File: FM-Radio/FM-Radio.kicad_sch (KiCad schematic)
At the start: 60 parts, among them J1 L_OUT, J2 USB_C_Receptacle_USB2.0, J3 R_OUT, J4 VBUS, J5 GND, J6 BWSMA-KE-Z001, SW2 EN, U2 SI4702-C19-GMR, U3 ESP32-S3-MINI-1, U4 PRTR5V0U2X, U5 TPS62160DSG, U6 PAM8406D, Y1 32.768 kHz

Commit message: RAAAA
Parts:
- C1, C3: LCSC C15850 -> C440198
- C15: LCSC Part # C72498 -> C3340
- C23: LCSC Part # C15850 -> C440198
- C25: LCSC Part # C1791 -> C46653
- R10, R3: LCSC Part # C17414 -> C17673
- R2: LCSC Part # C84376 -> C17414
- U6: LCSC Part # (none) -> C86270
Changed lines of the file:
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@@
 			)
 		)
-		(property "LCSC Part #" "C15850"
+		(property "LCSC Part #" "C440198"
 			(at 200.66 130.81 0)
 			(effects
@@
 			)
 		)
-		(property "LCSC Part #" "C17414"
+		(property "LCSC Part #" "C17673"
 			(at 81.28 156.21 0)
 			(effects
@@
 			)
 		)
-		(property "LCSC" "C15850"
+		(property "LCSC" "C440198"
 			(at 143.51 30.48 0)
 			(effects
@@
 			)
 		)
+		(property "LCSC Part #" "C86270"
+			(at 157.48 74.93 0)
+			(effects
+				(font
+					(size 1.27 1.27)
+				)
+				(hide yes)
+			)
+		)
 		(pin "5"
 		)
@@
 			)
 		)
-		(property "LCSC Part #" "C84376"
+		(property "LCSC Part #" "C17414"
 			(at 24.13 52.07 0)
 			(effects
@@
 			)
 		)
-		(property "LCSC Part #" "C72498"
+		(property "LCSC Part #" "C3340"
 			(at 130.81 30.48 0)
 			(effects
@@
 			)
 		)
-		(property "LCSC" "C15850"
+		(property "LCSC" "C440198"
 			(at 215.9 30.48 0)
 			(effects
@@
 			)
 		)
-		(property "LCSC Part #" "C1791"
+		(property "LCSC Part #" "C46653"
 			(at 15.24 33.02 0)
 			(effects
@@
 			)
 		)
-		(property "LCSC Part #" "C17414"
+		(property "LCSC Part #" "C17673"
 			(at 88.9 158.75 0)
 			(effects

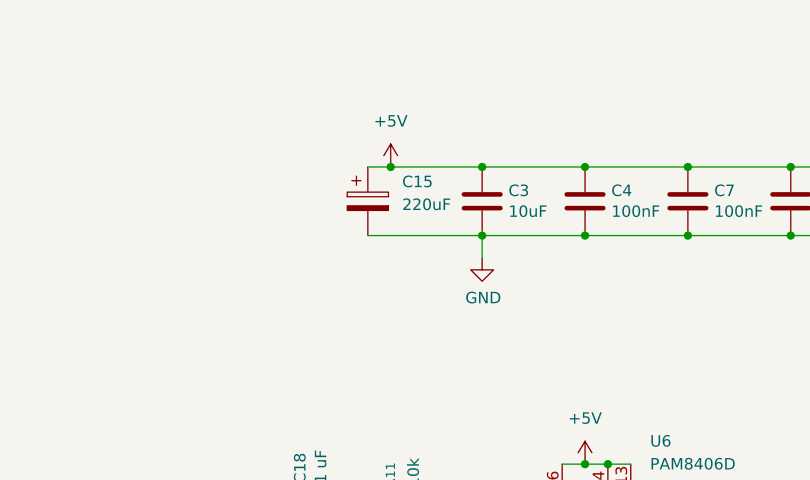
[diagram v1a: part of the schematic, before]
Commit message: FM radio
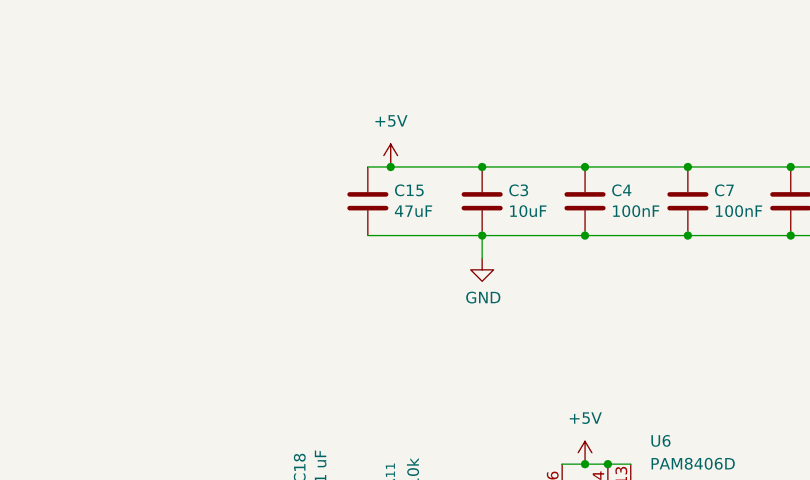
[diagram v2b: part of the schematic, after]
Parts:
- removed C15: 220uF, Capacitor_SMD:C_Elec_8x10.2, symbol Device:C_Polarized
- added C15: 47uF, Capacitor_SMD:C_1206_3216Metric, symbol Device:C
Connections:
- net +5V: now also C15.1
- net GND: now also C15.2
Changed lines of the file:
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@@
+	)
+	(symbol
+		(lib_id "Device:C")
+		(at 130.81 30.48 0)
+		(unit 1)
+		(exclude_from_sim no)
+		(in_bom yes)
+		(on_board yes)
+		(dnp no)
+		(property "Reference" "C15"
+			(at 133.731 29.3116 0)
+			(effects
+				(font
+					(size 1.27 1.27)
+				)
+				(justify left)
+			)
+		)
+		(property "Value" "47uF"
+			(at 133.731 31.623 0)
+			(effects
+				(font
+					(size 1.27 1.27)
+				)
+				(justify left)
+			)
+		)
+		(property "Footprint" "Capacitor_SMD:C_1206_3216Metric"
+			(at 131.7752 34.29 0)
+			(effects
+				(font
+					(size 1.27 1.27)
+				)
+				(hide yes)
+			)
+		)
+		(property "Datasheet" "~"
+			(at 130.81 30.48 0)
+			(effects
+				(font
+					(size 1.27 1.27)
+				)
+				(hide yes)
+			)
+		)
+		(property "Description" ""
+			(at 130.81 30.48 0)
+			(effects
+				(font
+					(size 1.27 1.27)
+				)
+			)
+		)
+		(property "LCSC" "C96123"
+			(at 130.81 30.48 0)
+			(effects
+				(font
+					(size 1.27 1.27)
+				)
+				(hide yes)
+			)
+		)
+		(property "JlcRotOffset" ""
+			(at 130.81 30.48 0)
+			(effects
+				(font
+					(size 1.27 1.27)
+				)
+				(hide yes)
+			)
+		)
+		(pin "1"
+		)
+		(pin "2"
+		)
+		(instances
+			(project "FM-Radio"
+				(path "/8a5dac2c-def6-4068-997d-88e941bc9e21"
+					(reference "C15")
+					(unit 1)
+				)
+			)
+		)
 	)
 	(symbol
@@
 					(unit 1)
 				)
-			)
-		)
-	)
-	(symbol
-		(lib_id "Device:C_Polarized")
-		(at 130.81 30.48 0)
-		(unit 1)
-		(exclude_from_sim no)
-		(in_bom yes)
-		(on_board yes)
-		(dnp no)
-		(fields_autoplaced yes)
-		(property "Reference" "C15"
-			(at 134.62 28.3209 0)
-			(effects
-				(font
-					(size 1.27 1.27)
-				)
-				(justify left)
-			)
-		)
-		(property "Value" "220uF"
-			(at 134.62 30.8609 0)
-			(effects
-				(font
-					(size 1.27 1.27)
-				)
-				(justify left)
-			)
-		)
-		(property "Footprint" "Capacitor_SMD:C_Elec_8x10.2"
-			(at 131.7752 34.29 0)
-			(effects
-				(font
-					(size 1.27 1.27)
-				)
-				(hide yes)
-			)
-		)
-		(property "Datasheet" "~"
-			(at 130.81 30.48 0)
-			(effects
-				(font
-					(size 1.27 1.27)
-				)
-				(hide yes)
-			)
-		)
-		(property "Description" "Polarized capacitor"
-			(at 130.81 30.48 0)
-			(effects
-				(font
-					(size 1.27 1.27)
-				)
-				(hide yes)
-			)
-		)
-		(property "LCSC Part #" "C3340"
-			(at 130.81 30.48 0)
-			(effects
-				(font
-					(size 1.27 1.27)
-				)
-				(hide yes)
-			)
-		)
-		(pin "1"
-		)
-		(pin "2"
-		)
-		(instances
-			(project ""
-				(path "/8a5dac2c-def6-4068-997d-88e941bc9e21"
-					(reference "C15")
-					(unit 1)
-				)

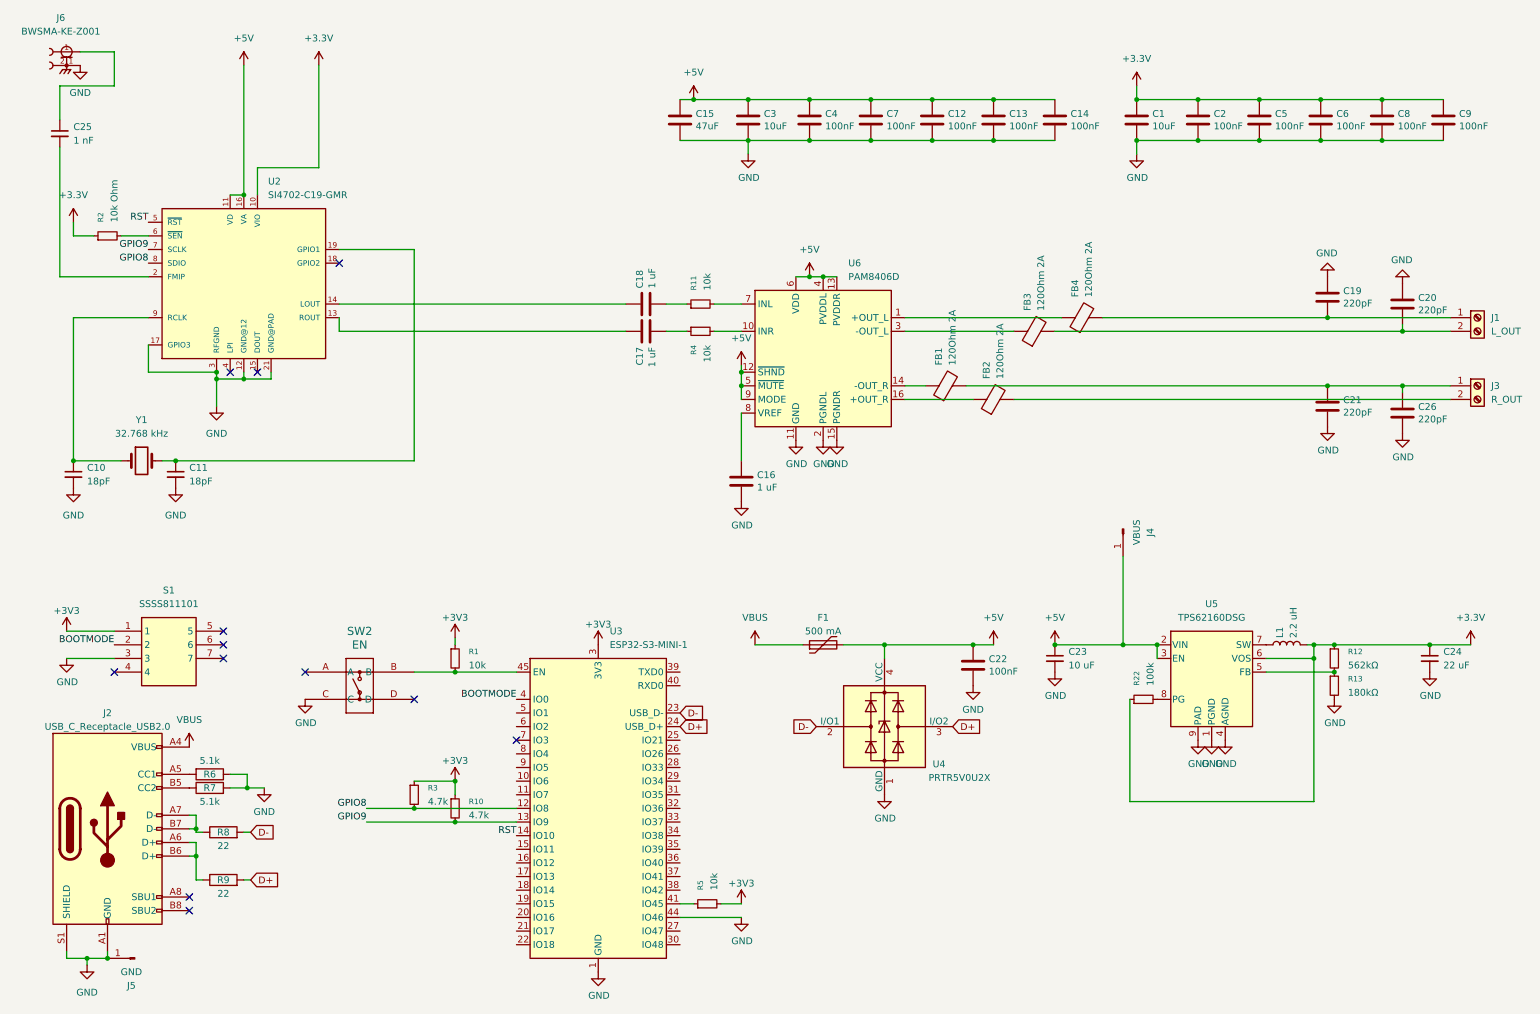
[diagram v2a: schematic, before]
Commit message: Smaller components
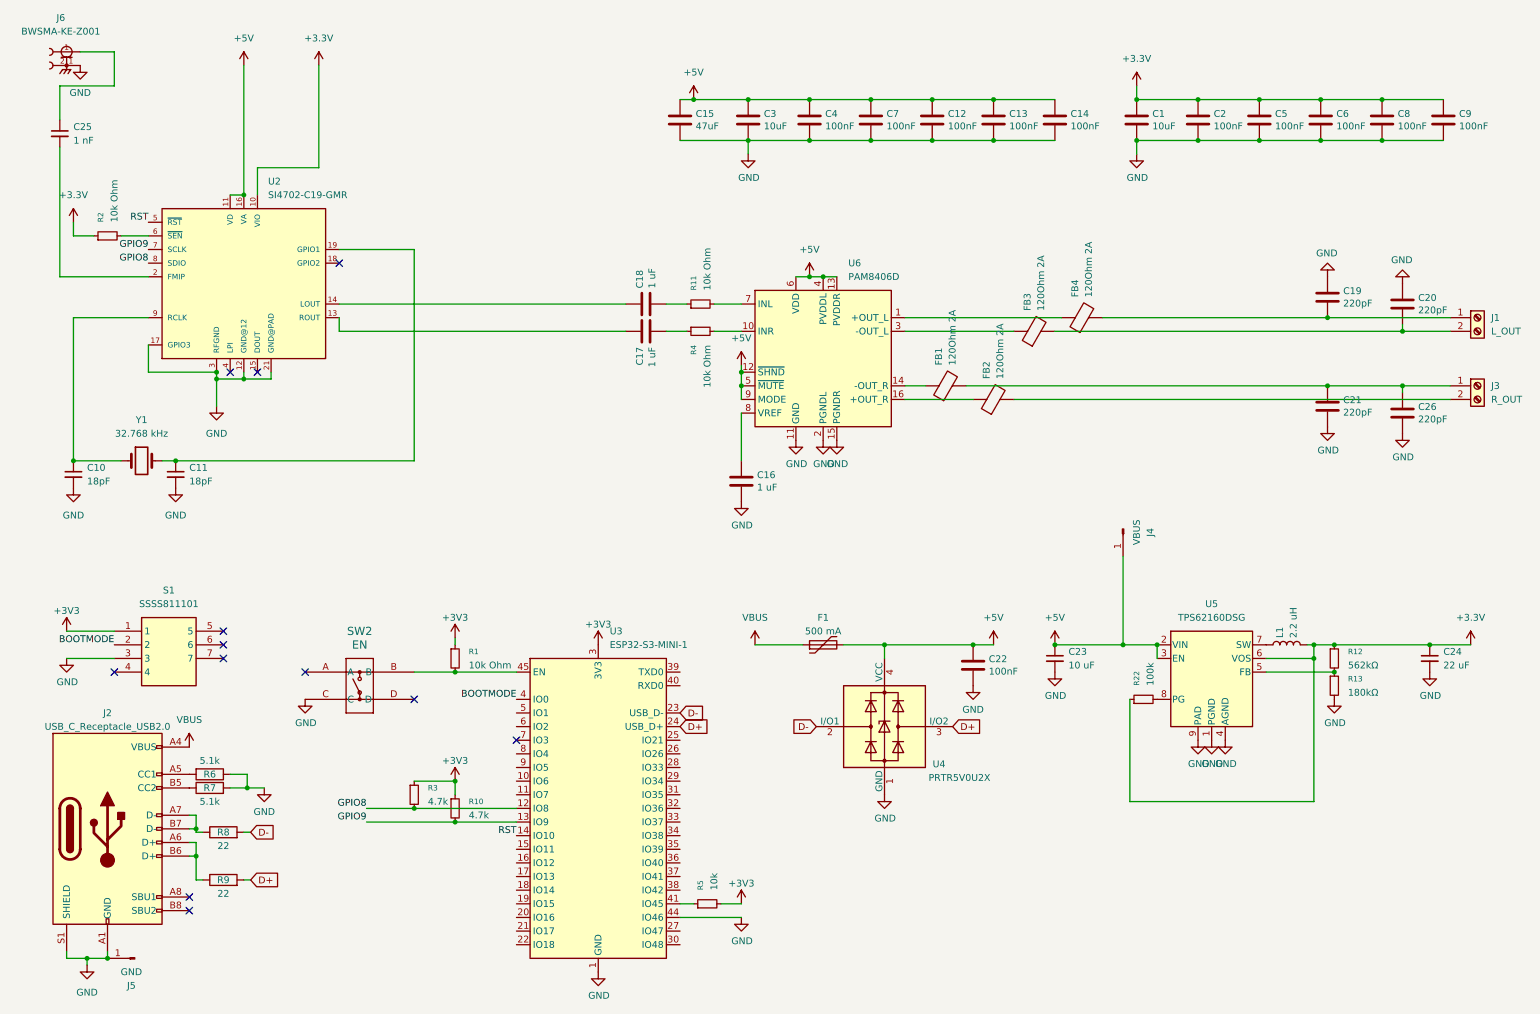
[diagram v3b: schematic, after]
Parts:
- C1, C3: footprint Capacitor_SMD:C_0805_2012Metric -> Capacitor_SMD:C_0603_1608Metric; LCSC C440198 -> C19702
- C12, C13, C14, C2, C4, C5, C6, C7, C8, C9: footprint Capacitor_SMD:C_0805_2012Metric -> Capacitor_SMD:C_0603_1608Metric; LCSC C28233 -> C14663
- R1, R11, R4: value 10k -> 10k Ohm; footprint Resistor_SMD:R_0805_2012Metric -> Resistor_SMD:R_0603_1608Metric; LCSC Part # C17414 -> C98220
- R2: footprint Resistor_SMD:R_0805_2012Metric -> Resistor_SMD:R_0603_1608Metric; LCSC Part # C17414 -> C98220

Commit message: go go gadget routing
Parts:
- removed C23: 10 uF, Capacitor_SMD:C_0805_2012Metric, symbol Device:C_Small
- added C23: 10uF, Capacitor_SMD:C_0603_1608Metric, symbol Device:C
- C10, C11: footprint Capacitor_SMD:C_0805_2012Metric -> Capacitor_SMD:C_0603_1608Metric; LCSC Part # C113825 -> C1647
- C16, C17, C18: footprint Capacitor_SMD:C_0805_2012Metric -> Capacitor_SMD:C_0603_1608Metric; LCSC Part # C28323 -> C29936
- C19, C20, C21, C26: footprint Capacitor_SMD:C_0805_2012Metric -> Capacitor_SMD:C_0603_1608Metric; LCSC C107145 -> C1603
- C22: footprint Capacitor_SMD:C_0805_2012Metric -> Capacitor_SMD:C_0603_1608Metric; LCSC C28233 -> C14663
- C24: footprint Capacitor_SMD:C_0805_2012Metric -> Capacitor_SMD:C_0603_1608Metric; LCSC Part # C45783 -> C86295
- C25: footprint Capacitor_SMD:C_0805_2012Metric -> Capacitor_SMD:C_0603_1608Metric; LCSC Part # C46653 -> C1588
- R10, R3: footprint Resistor_SMD:R_0805_2012Metric -> Resistor_SMD:R_0603_1608Metric; LCSC Part # C17673 -> C99782
- R22: footprint Resistor_SMD:R_0805_2012Metric -> Resistor_SMD:R_0603_1608Metric; LCSC Part # C149504 -> C14675
- R5: value 10k -> 10k Ohm; footprint Resistor_SMD:R_0805_2012Metric -> Resistor_SMD:R_0603_1608Metric; LCSC Part # C17414 -> C98220
- R6, R7: footprint Resistor_SMD:R_0805_2012Metric -> Resistor_SMD:R_0603_1608Metric; LCSC Part # C27834 -> C23186
- R8, R9: footprint Resistor_SMD:R_0805_2012Metric -> Resistor_SMD:R_0603_1608Metric; LCSC Part # C17561 -> C23345
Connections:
- net +5V: now also C23.1
- net GND: now also C23.2

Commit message: Yarrr harrr
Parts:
- removed U3: ESP32-S3-MINI-1, RF_Module:ESP32-S2-MINI-1, symbol RF_Module:ESP32-S3-MINI-1
- added U1: ESP32-S3-MINI-1U, RF_Module:ESP32-S2-MINI-1U, symbol RF_Module:ESP32-S3-MINI-1U
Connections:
- net +3V3: now also U1.3 (3V3)
- net BOOTMODE: now also U1.4 (IO0)
- net D+: now also U1.24 (USB_D+)
- net D-: now also U1.23 (USB_D-)
- net GND: now also U1.1 (GND), U1.2 (GND), U1.42 (GND), U1.43 (GND), U1.44 (IO46), U1.46 (GND), U1.47 (GND), U1.48 (GND), U1.49 (GND), U1.50 (GND), U1.51 (GND), U1.52 (GND), U1.53 (GND), U1.54 (GND), U1.55 (GND), U1.56 (GND), U1.57 (GND), U1.58 (GND), U1.59 (GND), U1.60 (GND), U1.61 (GND), U1.62 (GND), U1.63 (GND), U1.64 (GND), U1.65 (GND)
- net GPIO8: now also U1.12 (IO8)
- net GPIO9: now also U1.13 (IO9)
- net RST: now also U1.14 (IO10)
- net at R1.2, SW2.B: now also U1.45 (EN)
- net at R5.1: now also U1.41 (IO45)
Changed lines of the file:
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@@
-	)
-	(symbol
-		(lib_id "RF_Module:ESP32-S3-MINI-1")
-		(at 115.57 158.75 0)
-		(unit 1)
-		(exclude_from_sim no)
-		(in_bom yes)
-		(on_board yes)
-		(dnp no)
-		(fields_autoplaced yes)
-		(property "Reference" "U3"
-			(at 117.7133 125.73 0)
-			(effects
-				(font
-					(size 1.27 1.27)
-				)
-				(justify left)
-			)
-		)
-		(property "Value" "ESP32-S3-MINI-1"
-			(at 117.7133 128.27 0)
-			(effects
-				(font
-					(size 1.27 1.27)
-				)
-				(justify left)
-			)
-		)
-		(property "Footprint" "RF_Module:ESP32-S2-MINI-1"
-			(at 130.81 187.96 0)
-			(effects
-				(font
-					(size 1.27 1.27)
-				)
-				(hide yes)
-			)
-		)
-		(property "Datasheet" "https://www.espressif.com/sites/default/files/documentation/esp32-s3-mini-1_mini-1u_datasheet_en.pdf"
-			(at 115.57 118.11 0)
-			(effects
-				(font
-					(size 1.27 1.27)
-				)
-				(hide yes)
-			)
-		)
-		(property "Description" "RF Module, ESP32-S3 SoC, Wi-Fi 802.11b/g/n, Bluetooth, BLE, 32-bit, 3.3V, SMD, onboard antenna"
-			(at 115.57 115.57 0)
-			(effects
-				(font
-					(size 1.27 1.27)
-				)
-				(hide yes)
-			)
-		)
-		(property "LCSC Part #" "C2913206 "
-			(at 115.57 158.75 0)
-			(effects
-				(font
-					(size 1.27 1.27)
-				)
-				(hide yes)
-			)
-		)
-		(pin "56"
-		)
-		(pin "55"
-		)
-		(pin "54"
-		)
-		(pin "53"
-		)
-		(pin "51"
-		)
-		(pin "52"
-		)
-		(pin "50"
-		)
-		(pin "49"
-		)
-		(pin "48"
-		)
-		(pin "47"
-		)
-		(pin "46"
-		)
-		(pin "43"
-		)
-		(pin "42"
-		)
-		(pin "2"
-		)
-		(pin "1"
-		)
-		(pin "3"
-		)
-		(pin "22"
-		)
-		(pin "21"
-		)
-		(pin "20"
-		)
-		(pin "19"
-		)
-		(pin "18"
-		)
-		(pin "59"
-		)
-		(pin "28"
-		)
-		(pin "31"
-		)
-		(pin "40"
-		)
-		(pin "61"
-		)
-		(pin "23"
-		)
-		(pin "32"
-		)
-		(pin "62"
-		)
-		(pin "60"
-		)
-		(pin "24"
-		)
-		(pin "39"
-		)
-		(pin "25"
-		)
-		(pin "29"
-		)
-		(pin "57"
-		)
-		(pin "26"
-		)
-		(pin "58"
-		)
-		(pin "64"
-		)
-		(pin "34"
-		)
-		(pin "65"
-		)
-		(pin "63"
-		)
-		(pin "33"
-		)
-		(pin "27"
-		)
-		(pin "37"
-		)
-		(pin "35"
-		)
-		(pin "38"
-		)
-		(pin "44"
-		)
-		(pin "36"
-		)
-		(pin "41"
-		)
-		(pin "30"
-		)
-		(pin "13"
-		)
-		(pin "12"
-		)
-		(pin "11"
-		)
-		(pin "10"
-		)
-		(pin "9"
-		)
-		(pin "8"
-		)
-		(pin "7"
-		)
-		(pin "6"
-		)
-		(pin "4"
-		)
-		(pin "45"
-		)
-		(pin "5"
-		)
-		(pin "15"
-		)
-		(pin "16"
-		)
-		(pin "14"
-		)
-		(pin "17"
-		)
-		(instances
-			(project "FM-Radio"
-				(path "/8a5dac2c-def6-4068-997d-88e941bc9e21"
-					(reference "U3")
-					(unit 1)
-				)
-			)
-		)
 	)
 	(symbol
@@
 					(unit 1)
 				)
+			)
+		)
+	)
+	(symbol
+		(lib_id "RF_Module:ESP32-S3-MINI-1U")
+		(at 115.57 158.75 0)
+		(unit 1)
+		(exclude_from_sim no)
+		(in_bom yes)
+		(on_board yes)
+		(dnp no)
+		(fields_autoplaced yes)
+		(property "Reference" "U1"
+			(at 117.7133 125.73 0)
+			(effects
+				(font
+					(size 1.27 1.27)
+				)
+				(justify left)
+			)
+		)
+		(property "Value" "ESP32-S3-MINI-1U"
+			(at 117.7133 128.27 0)
+			(effects
+				(font
+					(size 1.27 1.27)
+				)
+				(justify left)
+			)
+		)
+		(property "Footprint" "RF_Module:ESP32-S2-MINI-1U"
+			(at 132.08 187.96 0)
+			(effects
+				(font
+					(size 1.27 1.27)
+				)
+				(hide yes)
+			)
+		)
+		(property "Datasheet" "https://www.espressif.com/sites/default/files/documentation/esp32-s3-mini-1_mini-1u_datasheet_en.pdf"
+			(at 115.57 118.11 0)
+			(effects
+				(font
+					(size 1.27 1.27)
+				)
+				(hide yes)
+			)
+		)
+		(property "Description" "RF Module, ESP32-S3 SoC, Wi-Fi 802.11b/g/n, Bluetooth, BLE, 32-bit, 3.3V, SMD, external antenna"
+			(at 115.57 115.57 0)
+			(effects
+				(font
+					(size 1.27 1.27)
+				)
+				(hide yes)
+			)
+		)
+		(pin "60"
+		)
+		(pin "61"
+		)
+		(pin "42"
+		)
+		(pin "2"
+		)
+		(pin "45"
+		)
+		(pin "21"
+		)
+		(pin "20"
+		)
+		(pin "19"
+		)
+		(pin "18"
+		)
+		(pin "17"
+		)
+		(pin "16"
+		)
+		(pin "15"
+		)
+		(pin "14"
+		)
+		(pin "13"
+		)
+		(pin "12"
+		)
+		(pin "11"
+		)
+		(pin "10"
+		)
+		(pin "8"
+		)
+		(pin "22"
+		)
+		(pin "5"
+		)
+		(pin "4"
+		)
+		(pin "6"
+		)
+		(pin "7"
+		)
+		(pin "9"
+		)
+		(pin "56"
+		)
+		(pin "49"
+		)
+		(pin "54"
+		)
+		(pin "52"
+		)
+		(pin "53"
+		)
+		(pin "50"
+		)
+		(pin "51"
+		)
+		(pin "58"
+		)
+		(pin "57"
+		)
+		(pin "55"
+		)
+		(pin "59"
+		)
+		(pin "48"
+		)
+		(pin "46"
+		)
+		(pin "47"
+		)
+		(pin "43"
+		)
+		(pin "1"
+		)
+		(pin "3"
+		)
+		(pin "44"
+		)
+		(pin "37"
+		)
+		(pin "27"
+		)
+		(pin "30"
+		)
+		(pin "38"
+		)
+		(pin "41"
+		)
+		(pin "36"
+		)
+		(pin "32"
+		)
+		(pin "34"
+		)
+		(pin "62"
+		)
+		(pin "33"
+		)
+		(pin "35"
+		)
+		(pin "31"
+		)
+		(pin "40"
+		)
+		(pin "39"
+		)
+		(pin "23"
+		)
+		(pin "24"
+		)
+		(pin "28"
+		)
+		(pin "25"
+		)
+		(pin "29"
+		)
+		(pin "65"
+		)
+		(pin "63"
+		)
+		(pin "26"
+		)
+		(pin "64"
+		)
+		(instances
+			(project ""
+				(path "/8a5dac2c-def6-4068-997d-88e941bc9e21"
+					(reference "U1")
+					(unit 1)
+				)
